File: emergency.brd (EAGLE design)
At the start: 67.5 x 88.5 mm, 33 parts, among them J1 8P8C, J6 MA02-2, Q2 BUZ11BH, U1 V23134J1052D642, U2 V23134J1052D642, U3 AP65111AWU-7, U4 TLP184

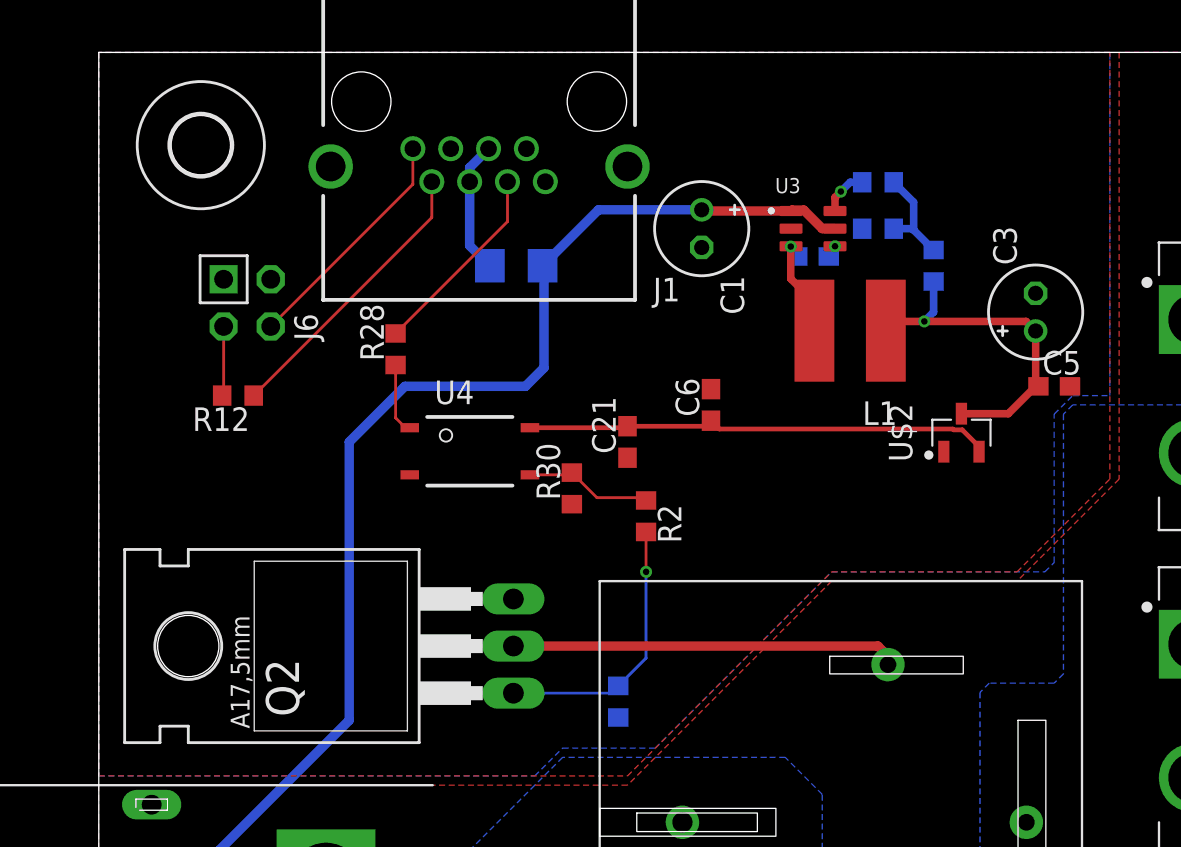
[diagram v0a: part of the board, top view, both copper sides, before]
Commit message: GNDIOのベタにビアを打った
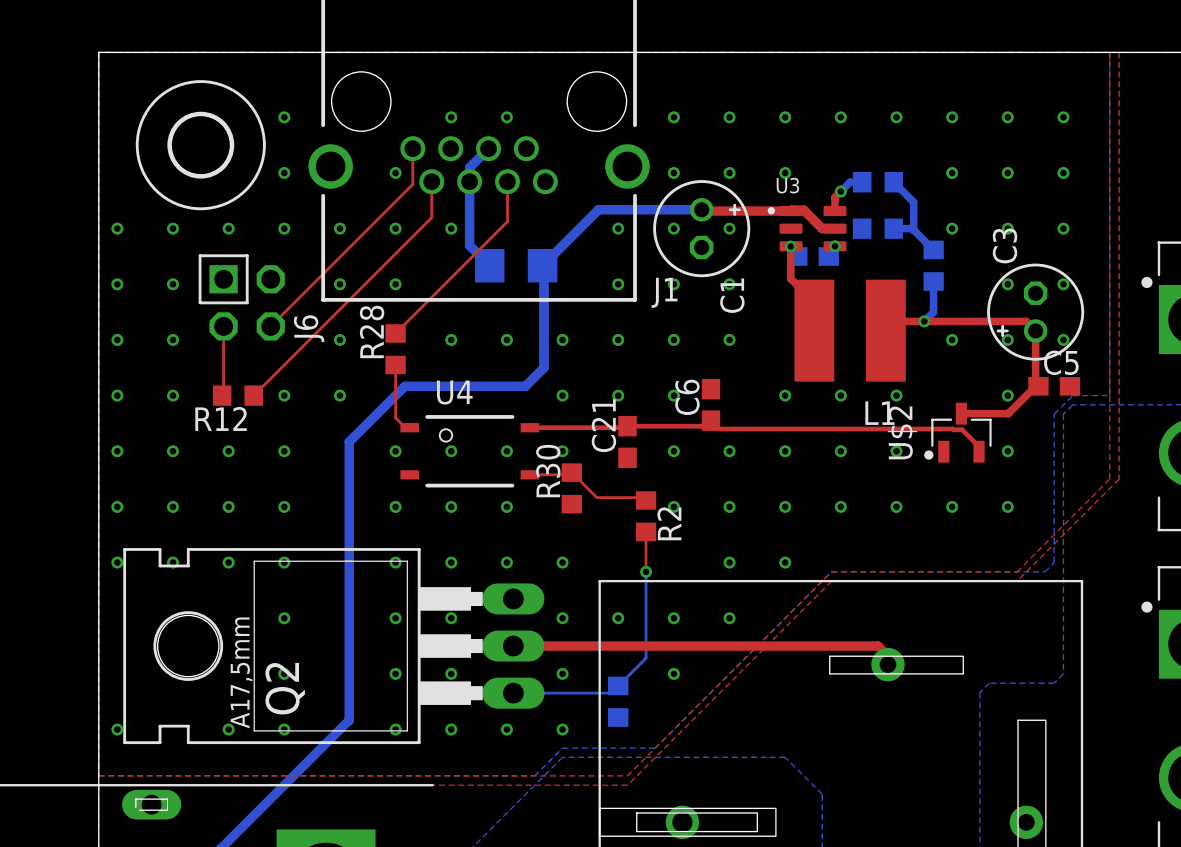
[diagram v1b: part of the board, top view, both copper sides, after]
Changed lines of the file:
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@@
 <setting verticaltext="up"/>
 </settings>
-<grid distance="0.5" unitdist="mm" unit="mm" style="lines" multiple="1" display="yes" altdistance="0.1" altunitdist="mm" altunit="mm"/>
+<grid distance="3" unitdist="mm" unit="mm" style="lines" multiple="1" display="yes" altdistance="0.1" altunitdist="mm" altunit="mm"/>
 <layers>
 <layer number="1" name="Top" color="4" fill="1" visible="yes" active="yes"/>
@@
 <contactref element="C21" pad="1"/>
 <contactref element="U4" pad="2"/>
+<via x="1" y="79" extent="1-16" drill="0.35"/>
+<via x="1" y="76" extent="1-16" drill="0.35"/>
+<via x="4" y="76" extent="1-16" drill="0.35"/>
+<via x="1" y="73" extent="1-16" drill="0.35"/>
+<via x="4" y="73" extent="1-16" drill="0.35"/>
+<via x="4" y="70" extent="1-16" drill="0.35"/>
+<via x="1" y="70" extent="1-16" drill="0.35"/>
+<via x="1" y="67" extent="1-16" drill="0.35"/>
+<via x="4" y="67" extent="1-16" drill="0.35"/>
+<via x="7" y="67" extent="1-16" drill="0.35"/>
+<via x="7" y="64" extent="1-16" drill="0.35"/>
+<via x="4" y="64" extent="1-16" drill="0.35"/>
+<via x="1" y="64" extent="1-16" drill="0.35"/>
+<via x="1" y="61" extent="1-16" drill="0.35"/>
+<via x="7" y="61" extent="1-16" drill="0.35"/>
+<via x="4" y="61" extent="1-16" drill="0.35"/>
+<via x="1" y="52" extent="1-16" drill="0.35"/>
+<via x="7" y="52" extent="1-16" drill="0.35"/>
+<via x="10" y="52" extent="1-16" drill="0.35"/>
+<via x="10" y="55" extent="1-16" drill="0.35"/>
+<via x="10" y="58" extent="1-16" drill="0.35"/>
+<via x="10" y="61" extent="1-16" drill="0.35"/>
+<via x="10" y="64" extent="1-16" drill="0.35"/>
+<via x="10" y="67" extent="1-16" drill="0.35"/>
+<via x="10" y="70" extent="1-16" drill="0.35"/>
+<via x="13" y="70" extent="1-16" drill="0.35"/>
+<via x="13" y="73" extent="1-16" drill="0.35"/>
+<via x="13" y="76" extent="1-16" drill="0.35"/>
+<via x="13" y="79" extent="1-16" drill="0.35"/>
+<via x="10" y="79" extent="1-16" drill="0.35"/>
+<via x="10" y="82" extent="1-16" drill="0.35"/>
+<via x="10" y="85" extent="1-16" drill="0.35"/>
+<via x="16" y="82" extent="1-16" drill="0.35"/>
+<via x="19" y="85" extent="1-16" drill="0.35"/>
+<via x="22" y="85" extent="1-16" drill="0.35"/>
+<via x="19" y="79" extent="1-16" drill="0.35"/>
+<via x="16" y="79" extent="1-16" drill="0.35"/>
+<via x="16" y="76" extent="1-16" drill="0.35"/>
+<via x="19" y="73" extent="1-16" drill="0.35"/>
+<via x="22" y="73" extent="1-16" drill="0.35"/>
+<via x="16" y="67" extent="1-16" drill="0.35"/>
+<via x="22" y="67" extent="1-16" drill="0.35"/>
+<via x="19" y="67" extent="1-16" drill="0.35"/>
+<via x="16" y="64" extent="1-16" drill="0.35"/>
+<via x="19" y="64" extent="1-16" drill="0.35"/>
+<via x="16" y="61" extent="1-16" drill="0.35"/>
+<via x="19" y="61" extent="1-16" drill="0.35"/>
+<via x="16" y="58" extent="1-16" drill="0.35"/>
+<via x="19" y="58" extent="1-16" drill="0.35"/>
+<via x="16" y="55" extent="1-16" drill="0.35"/>
+<via x="19" y="55" extent="1-16" drill="0.35"/>
+<via x="19" y="52" extent="1-16" drill="0.35"/>
+<via x="16" y="52" extent="1-16" drill="0.35"/>
+<via x="22" y="52" extent="1-16" drill="0.35"/>
+<via x="25" y="52" extent="1-16" drill="0.35"/>
+<via x="25" y="55" extent="1-16" drill="0.35"/>
+<via x="31" y="55" extent="1-16" drill="0.35"/>
+<via x="31" y="58" extent="1-16" drill="0.35"/>
+<via x="28" y="58" extent="1-16" drill="0.35"/>
+<via x="25" y="58" extent="1-16" drill="0.35"/>
+<via x="25" y="61" extent="1-16" drill="0.35"/>
+<via x="22" y="61" extent="1-16" drill="0.35"/>
+<via x="22" y="64" extent="1-16" drill="0.35"/>
+<via x="34" y="58" extent="1-16" drill="0.35"/>
+<via x="34" y="61" extent="1-16" drill="0.35"/>
+<via x="37" y="61" extent="1-16" drill="0.35"/>
+<via x="37" y="64" extent="1-16" drill="0.35"/>
+<via x="34" y="64" extent="1-16" drill="0.35"/>
+<via x="34" y="67" extent="1-16" drill="0.35"/>
+<via x="31" y="67" extent="1-16" drill="0.35"/>
+<via x="31" y="64" extent="1-16" drill="0.35"/>
+<via x="25" y="67" extent="1-16" drill="0.35"/>
+<via x="25" y="70" extent="1-16" drill="0.35"/>
+<via x="25" y="73" extent="1-16" drill="0.35"/>
+<via x="28" y="73" extent="1-16" drill="0.35"/>
+<via x="28" y="70" extent="1-16" drill="0.35"/>
+<via x="31" y="70" extent="1-16" drill="0.35"/>
+<via x="31" y="73" extent="1-16" drill="0.35"/>
+<via x="34" y="73" extent="1-16" drill="0.35"/>
+<via x="37" y="70" extent="1-16" drill="0.35"/>
+<via x="37" y="67" extent="1-16" drill="0.35"/>
+<via x="28" y="76" extent="1-16" drill="0.35"/>
+<via x="28" y="79" extent="1-16" drill="0.35"/>
+<via x="31" y="85" extent="1-16" drill="0.35"/>
+<via x="31" y="82" extent="1-16" drill="0.35"/>
+<via x="31" y="79" extent="1-16" drill="0.35"/>
+<via x="31" y="76" extent="1-16" drill="0.35"/>
+<via x="34" y="76" extent="1-16" drill="0.35"/>
+<via x="34" y="79" extent="1-16" drill="0.35"/>
+<via x="34" y="82" extent="1-16" drill="0.35"/>
+<via x="34" y="85" extent="1-16" drill="0.35"/>
+<via x="37" y="85" extent="1-16" drill="0.35"/>
+<via x="40" y="85" extent="1-16" drill="0.35"/>
+<via x="37" y="82" extent="1-16" drill="0.35"/>
+<via x="40" y="70" extent="1-16" drill="0.35"/>
+<via x="40" y="67" extent="1-16" drill="0.35"/>
+<via x="40" y="64" extent="1-16" drill="0.35"/>
+<via x="43" y="64" extent="1-16" drill="0.35"/>
+<via x="43" y="67" extent="1-16" drill="0.35"/>
+<via x="43" y="70" extent="1-16" drill="0.35"/>
+<via x="46" y="73" extent="1-16" drill="0.35"/>
+<via x="49" y="73" extent="1-16" drill="0.35"/>
+<via x="49" y="70" extent="1-16" drill="0.35"/>
+<via x="49" y="67" extent="1-16" drill="0.35"/>
+<via x="49" y="64" extent="1-16" drill="0.35"/>
+<via x="46" y="64" extent="1-16" drill="0.35"/>
+<via x="49" y="76" extent="1-16" drill="0.35"/>
+<via x="49" y="79" extent="1-16" drill="0.35"/>
+<via x="46" y="79" extent="1-16" drill="0.35"/>
+<via x="46" y="82" extent="1-16" drill="0.35"/>
+<via x="46" y="85" extent="1-16" drill="0.35"/>
+<via x="43" y="85" extent="1-16" drill="0.35"/>
+<via x="49" y="85" extent="1-16" drill="0.35"/>
+<via x="52" y="85" extent="1-16" drill="0.35"/>
+<via x="52" y="82" extent="1-16" drill="0.35"/>
+<via x="49" y="82" extent="1-16" drill="0.35"/>
+<via x="52" y="79" extent="1-16" drill="0.35"/>
+<via x="52" y="76" extent="1-16" drill="0.35"/>
+<via x="52" y="73" extent="1-16" drill="0.35"/>
 </signal>
 <signal name="N$7">
@@
 <contactref element="U1" pad="3"/>
 </signal>
+<signal name="N$11">
+<via x="4" y="79" extent="1-16" drill="0.35"/>
+<via x="7" y="79" extent="1-16" drill="0.35"/>
+<wire x1="4" y1="79" x2="7" y2="79" width="0" layer="19" extent="1-1"/>
+</signal>
 </signals>

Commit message: コイルの配線とベタの修正
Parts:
- U$11: value XT90PW_M -> XT90PW_F; device XT60_Connecotr:AMASS_XT90PW_M -> XT60_Connecotr:AMASS_XT90PW_F
- U$12, U$3, U$4, U$5: value XT60PW-F -> XT60PW-M; device XT60_Connecotr:AMASS_XT60PW_F -> XT60_Connecotr:AMASS_XT60PW_M
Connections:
- removed net N$4: U1.2, U2.1
- net +12V: now also U1.2
- net N$6: now also U2.1
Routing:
- net N$6: track 20.9 -> 54.9 mm
- net +12V: track 125.9 -> 159.9 mm
- removed copper zone on layer 16, net N$4
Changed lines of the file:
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@@
 <setting verticaltext="up"/>
 </settings>
-<grid distance="3" unitdist="mm" unit="mm" style="lines" multiple="1" display="yes" altdistance="0.1" altunitdist="mm" altunit="mm"/>
+<grid distance="0.5" unitdist="mm" unit="mm" style="lines" multiple="1" display="yes" altdistance="0.1" altunitdist="mm" altunit="mm"/>
 <layers>
 <layer number="1" name="Top" color="4" fill="1" visible="yes" active="yes"/>
@@
 <attribute name="VALUE" x="27.595" y="64.135" size="1.27" layer="27" rot="R270"/>
 </element>
-<element name="U$11" library="XT60_Connecotr" package="AMASS_XT90PW_M" value="XT90PW_M" x="10" y="38.5" smashed="yes" rot="R90">
+<element name="U$11" library="XT60_Connecotr" package="AMASS_XT90PW_F" value="XT90PW_F" x="10" y="38.5" smashed="yes" rot="R90">
 <attribute name="NAME" x="-9.2047" y="28.19658125" size="1.270559375" layer="25" rot="R90"/>
 <attribute name="VALUE" x="19.2177" y="28.18648125" size="1.2722" layer="27" rot="R90"/>
 </element>
-<element name="U$12" library="XT60_Connecotr" package="AMASS_XT60PW_F" value="XT60PW-F" x="65" y="70.5" smashed="yes" rot="R270">
+<element name="U$12" library="XT60_Connecotr" package="AMASS_XT60PW_M" value="XT60PW-M" x="65" y="70.5" smashed="yes" rot="R270">
 <attribute name="NAME" x="84.2047" y="80.80341875" size="1.270559375" layer="25" rot="R270"/>
 <attribute name="VALUE" x="55.7823" y="80.81351875" size="1.2722" layer="27" rot="R270"/>
@@
 <attribute name="VALUE" x="41.365" y="83.405" size="1.27" layer="28" rot="MR180"/>
 </element>
-<element name="U$3" library="XT60_Connecotr" package="AMASS_XT60PW_F" value="XT60PW-F" x="65" y="53" smashed="yes" rot="R270">
+<element name="U$3" library="XT60_Connecotr" package="AMASS_XT60PW_M" value="XT60PW-M" x="65" y="53" smashed="yes" rot="R270">
 <attribute name="NAME" x="84.2047" y="63.30341875" size="1.270559375" layer="25" rot="R270"/>
 <attribute name="VALUE" x="55.7823" y="63.31351875" size="1.2722" layer="27" rot="R270"/>
 </element>
 <element name="U2" library="relay" package="V23134J1052D642" value="V23134J1052D642" x="40" y="17.5" smashed="yes" rot="R270"/>
-<element name="U$4" library="XT60_Connecotr" package="AMASS_XT60PW_F" value="XT60PW-F" x="65" y="18" smashed="yes" rot="R270">
+<element name="U$4" library="XT60_Connecotr" package="AMASS_XT60PW_M" value="XT60PW-M" x="65" y="18" smashed="yes" rot="R270">
 <attribute name="NAME" x="84.2047" y="28.30341875" size="1.270559375" layer="25" rot="R270"/>
 <attribute name="VALUE" x="55.7823" y="28.31351875" size="1.2722" layer="27" rot="R270"/>
 </element>
-<element name="U$5" library="XT60_Connecotr" package="AMASS_XT60PW_F" value="XT60PW-F" x="65" y="35.5" smashed="yes" rot="R270">
+<element name="U$5" library="XT60_Connecotr" package="AMASS_XT60PW_M" value="XT60PW-M" x="65" y="35.5" smashed="yes" rot="R270">
 <attribute name="NAME" x="84.2047" y="45.80341875" size="1.270559375" layer="25" rot="R270"/>
 <attribute name="VALUE" x="55.7823" y="45.81351875" size="1.2722" layer="27" rot="R270"/>
@@
 <vertex x="67.5" y="0"/>
 <vertex x="67.5" y="88.5"/>
-<vertex x="55" y="88.5"/>
-<vertex x="55" y="65.5"/>
+<vertex x="54" y="88.5"/>
+<vertex x="54" y="69.5"/>
+<vertex x="53" y="68.5"/>
+<vertex x="51" y="68.5"/>
+<vertex x="50.5" y="68"/>
+<vertex x="50.5" y="61"/>
 <vertex x="49.5" y="60"/>
 <vertex x="39.5" y="60"/>
@@
 <vertex x="39.5" y="60.5"/>
 <vertex x="49.5" y="60.5"/>
-<vertex x="54.5" y="65.5"/>
-<vertex x="54.5" y="88.5"/>
+<vertex x="50" y="61"/>
+<vertex x="50" y="68.5"/>
+<vertex x="50.5" y="69"/>
+<vertex x="53" y="69"/>
+<vertex x="53.5" y="69.5"/>
+<vertex x="53.5" y="88.5"/>
 </polygon>
 <polygon width="0.1524" layer="16">
@@
 <vertex x="30" y="51"/>
 <vertex x="39.5" y="60.5"/>
-<vertex x="51" y="60.5"/>
-<vertex x="51.5" y="61"/>
+<vertex x="49.5" y="60.5"/>
+<vertex x="51.5" y="62.5"/>
 <vertex x="51.5" y="69"/>
 <vertex x="52.5" y="70"/>
-<vertex x="54.5" y="70"/>
-<vertex x="54.5" y="88.5"/>
+<vertex x="53.5" y="70"/>
+<vertex x="53.5" y="88.5"/>
 </polygon>
 <contactref element="R30" pad="1"/>
@@
 <contactref element="U3" pad="5"/>
 <contactref element="F1" pad="1"/>
-<contactref element="U2" pad="2"/>
 <wire x1="23.922" y1="77" x2="26.938" y2="80.016" width="0.508" layer="16"/>
 <wire x1="26.938" y1="80.016" x2="32.5" y2="80.016" width="0.508" layer="16"/>
@@
 <wire x1="38" y1="80" x2="37.365" y2="80" width="0.508" layer="1"/>
 <wire x1="37.365" y1="80" x2="37.315" y2="79.95" width="0.508" layer="1"/>
-<wire x1="42.54" y1="9" x2="18" y2="9" width="0.508" layer="16"/>
 <wire x1="13.5" y1="52.5" x2="13.5" y2="67.5" width="0.508" layer="16"/>
 <wire x1="13.5" y1="67.5" x2="16.5" y2="70.5" width="0.508" layer="16"/>
@@
 <wire x1="16.5" y1="70.5" x2="23" y2="70.5" width="0.508" layer="16"/>
 <wire x1="24" y1="71.5" x2="24" y2="76.922" width="0.508" layer="16"/>
+<contactref element="U2" pad="2"/>
+<contactref element="U1" pad="2"/>
+<wire x1="42.54" y1="9" x2="18" y2="9" width="0.508" layer="16"/>
+<wire x1="42.54" y1="9" x2="42.4946375" y2="17.5053625" width="0.508" layer="16"/>
+<wire x1="42.4946375" y1="17.5053625" x2="37" y2="23" width="0.508" layer="16"/>
+<wire x1="37" y1="23" x2="37" y2="30.5" width="0.508" layer="16"/>
+<wire x1="37" y1="30.5" x2="42.54" y2="36.04" width="0.508" layer="16"/>
+<wire x1="42.54" y1="36.04" x2="42.54" y2="38.5" width="0.508" layer="16"/>
 </signal>
 <signal name="N$1">
@@
 </polygon>
 </signal>
-<signal name="N$4">
-<contactref element="U2" pad="1"/>
-<contactref element="U1" pad="2"/>
-<polygon width="0.1524" layer="16">
-<vertex x="38" y="39.5"/>
-<vertex x="38" y="25"/>
-<vertex x="38" y="24.5"/>
-<vertex x="38.5" y="24"/>
-<vertex x="47.5" y="24"/>
-<vertex x="48" y="24.5"/>
-<vertex x="48" y="39.5"/>
-<vertex x="47.5" y="40"/>
-<vertex x="45.5" y="40"/>
-<vertex x="38.5" y="40"/>
-</polygon>
-</signal>
 <signal name="N$6">
 <contactref element="Q2" pad="D"/>
@@
 <wire x1="42.54" y1="55.96" x2="42" y2="56.5" width="0.508" layer="1"/>
 <wire x1="42" y1="56.5" x2="22.35" y2="56.5" width="0.508" layer="1"/>
+<contactref element="U2" pad="1"/>
+<wire x1="42.54" y1="55.5" x2="42.5" y2="47" width="0.508" layer="1"/>
+<wire x1="42.5" y1="47" x2="38" y2="42.5" width="0.508" layer="1"/>
+<wire x1="38" y1="42.5" x2="37" y2="41.5" width="0.508" layer="1"/>
+<wire x1="37" y1="41.5" x2="37" y2="35.5" width="0.508" layer="1"/>
+<wire x1="37" y1="35.5" x2="42.54" y2="29.96" width="0.508" layer="1"/>
+<wire x1="42.54" y1="29.96" x2="42.54" y2="26" width="0.508" layer="1"/>
 </signal>
 <signal name="OUT_POWER_A">

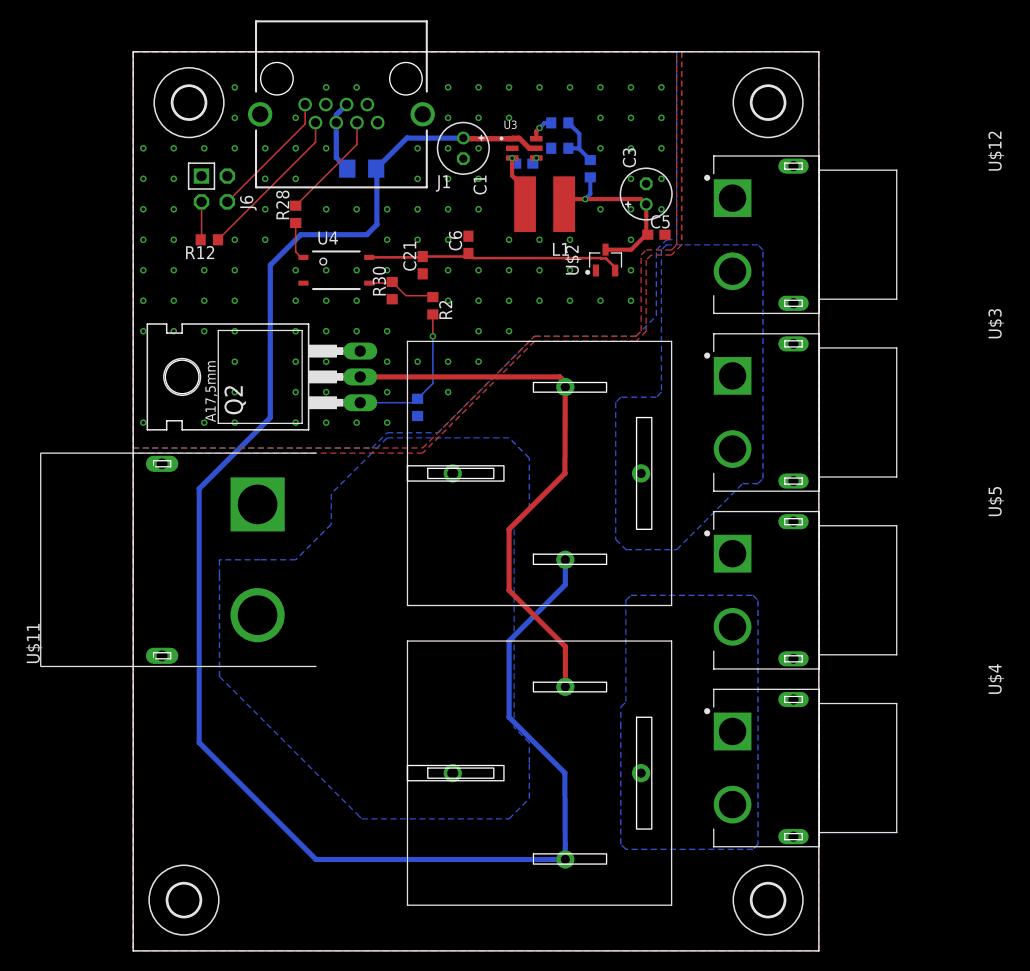
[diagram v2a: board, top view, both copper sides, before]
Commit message: リレーのライブラリの修正
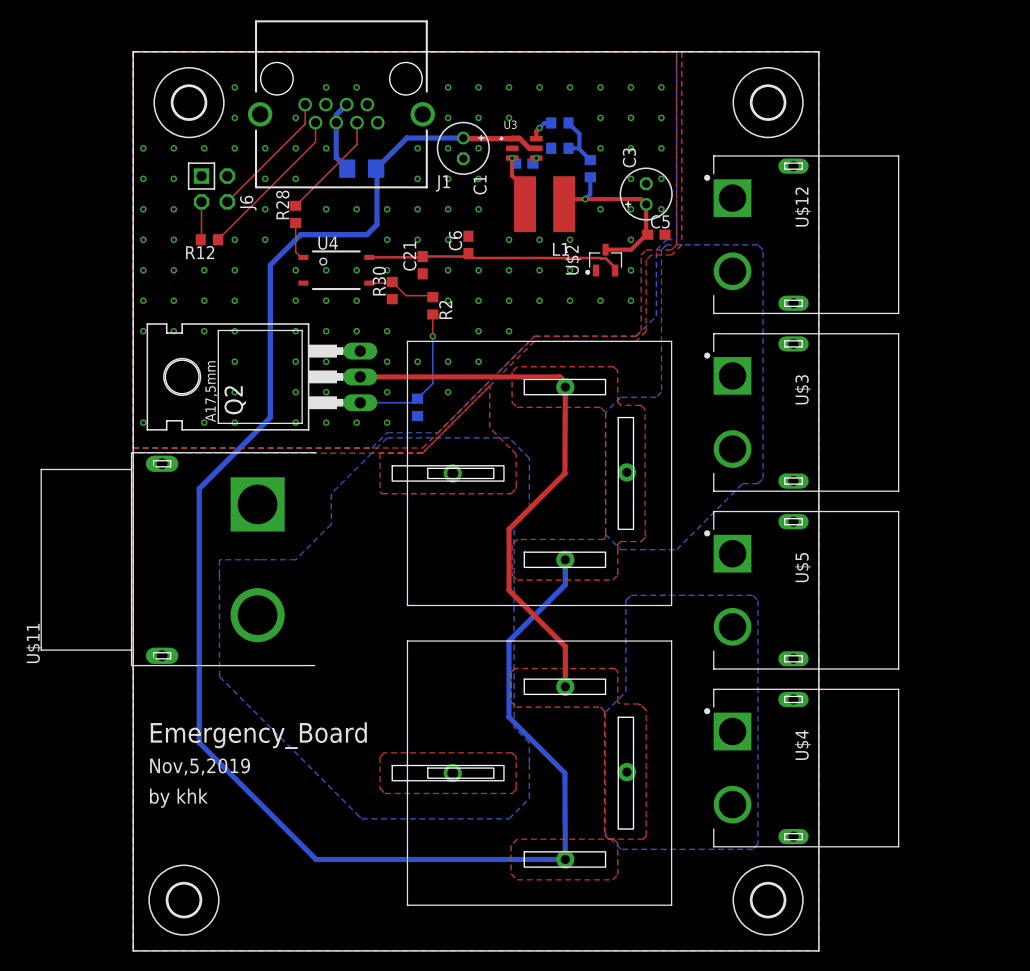
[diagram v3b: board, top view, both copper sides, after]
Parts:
- R2: value (none) -> 100R
- R3: value (none) -> 100k
- U$11: value XT90PW_F -> XT90PW_M; device XT60_Connecotr:AMASS_XT90PW_F -> XT60_Connecotr:AMASS_XT90PW_M
- U$12, U$3, U$4, U$5: value XT60PW-M -> XT60PW-F; device XT60_Connecotr:AMASS_XT60PW_M -> XT60_Connecotr:AMASS_XT60PW-F
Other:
- board text added: "Emergency_Board"
- board text added: "Nov,5,2019"
- board text added: "by khk"
